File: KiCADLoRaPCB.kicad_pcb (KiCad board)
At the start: 2 copper layers, 114.8 x 85.1 mm, 16 parts, among them J1 Raspberry_Pi_2_3, J2 RHF-GW, J3 Jack-DC, J9 RHF-GWx, M5 3.2mm

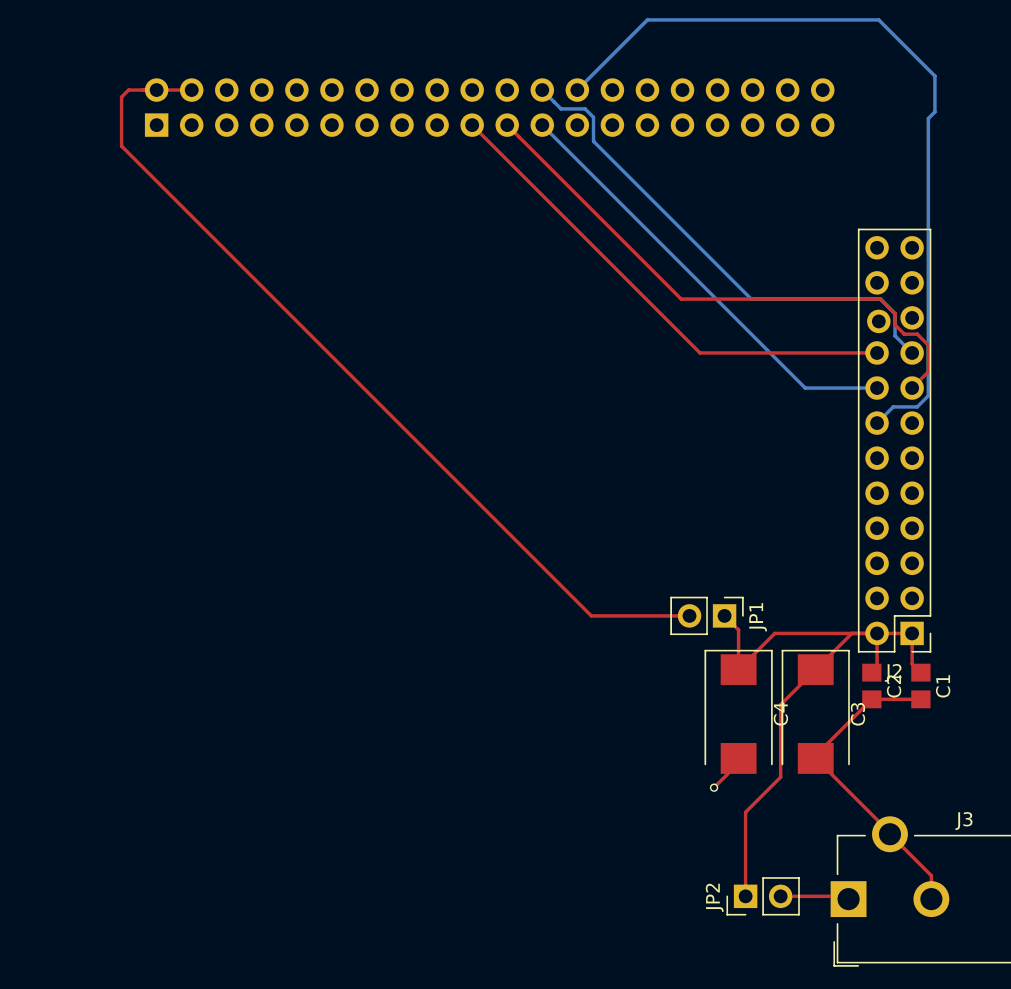
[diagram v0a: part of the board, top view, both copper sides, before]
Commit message: Finished tweaking the PWR plane and track width
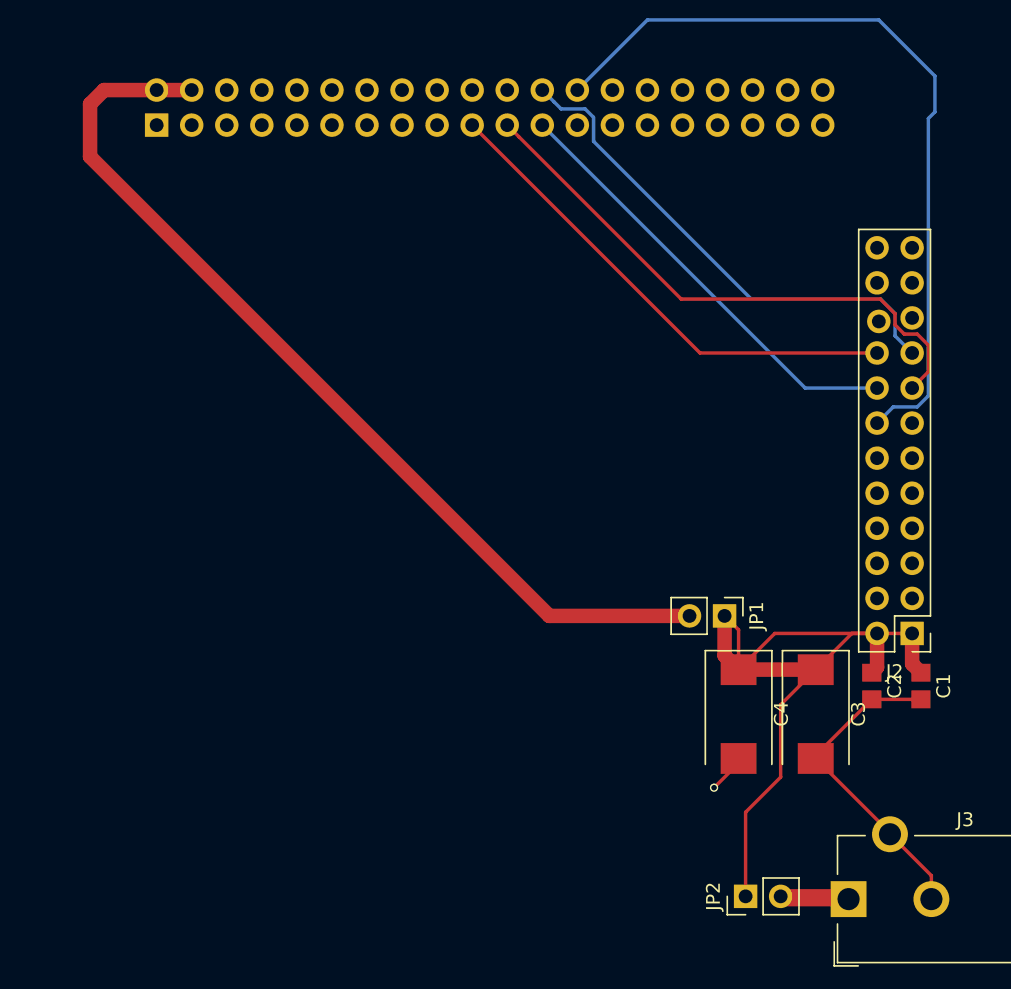
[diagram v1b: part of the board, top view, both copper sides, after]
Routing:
- net +5V: track 48.1 -> 59.5 mm
- net Net-(J3-Pad1): track 5.00 -> 10.3 mm
- net /5VR: track 65.6 -> 70.3 mm
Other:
- net class pwrr added: clearance 0.2, trace_width 1.05, via_dia 0.6, via_drill 0.4
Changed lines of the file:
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@@
     (thickness 1.6)
     (drawings 2970)
-    (tracks 69)
+    (tracks 77)
     (zones 0)
     (modules 16)
@@
     (uvia_dia 0.3)
     (uvia_drill 0.1)
-    (add_net +5V)
-    (add_net /5VR)
     (add_net GND)
     (add_net "Net-(J1-Pad1)")
@@
     (add_net "Net-(J2-Pad8)")
     (add_net "Net-(J2-Pad9)")
-    (add_net "Net-(J3-Pad1)")
   )
   (net_class SPI ""
@@
     (add_net "Net-(J1-Pad23)")
   )
+  (net_class pwrr ""
+    (clearance 0.2)
+    (trace_width 1.05)
+    (via_dia 0.6)
+    (via_drill 0.4)
+    (uvia_dia 0.3)
+    (uvia_drill 0.1)
+    (add_net +5V)
+    (add_net /5VR)
+    (add_net "Net-(J3-Pad1)")
+  )
   (module Connector_BarrelJack:BarrelJack_CUI_PJ-102AH_Horizontal placed (layer F.Cu)
     (at 137 114.5 90)
@@
   (gr_line (start 64.77 58.42) (end 60.96 58.42) (angle 90) (layer Edge.Cuts) (width 0.15))
   (gr_line (start 60.96 55.88) (end 64.77 55.88) (angle 90) (layer Edge.Cuts) (width 0.15))
+  (segment (start 129.032 97.8745) (end 134.62 97.8745) (width 1.05) (layer F.Cu) (net 1))
+  (segment (start 128.016 93.98) (end 128.016 96.8585) (width 1.05) (layer F.Cu) (net 1))
+  (segment (start 128.016 96.8585) (end 129.032 97.8745) (width 1.05) (layer F.Cu) (net 1))
+  (segment (start 141.605 95.25) (end 141.605 97.4575) (width 1.05) (layer F.Cu) (net 1))
+  (segment (start 141.605 97.4575) (end 142.24 98.0925) (width 1.05) (layer F.Cu) (net 1))
+  (segment (start 139.065 95.25) (end 139.065 97.7115) (width 1.05) (layer F.Cu) (net 1))
+  (segment (start 139.065 97.7115) (end 138.684 98.0925) (width 1.05) (layer F.Cu) (net 1))
   (segment (start 139.065 95.25) (end 141.605 95.25) (width 0.25) (layer F.Cu) (net 1))
   (segment (start 128.016 93.98) (end 129.032 94.996) (width 0.25) (layer F.Cu) (net 1))
   (segment (start 129.032 94.996) (end 129.032 97.8745) (width 0.25) (layer F.Cu) (net 1))
   (segment (start 129.54 114.3) (end 129.54 108.204) (width 0.25) (layer F.Cu) (net 1))
-  (segment (start 132.08 100.4145) (end 134.62 97.8745) (width 0.25) (layer F.Cu) (net 1))
-  (segment (start 132.08 105.664) (end 132.08 100.4145) (width 0.25) (layer F.Cu) (net 1))
   (segment (start 129.54 108.204) (end 132.08 105.664) (width 0.25) (layer F.Cu) (net 1))
+  (segment (start 132.08 105.664) (end 132.08 100.4145) (width 0.25) (layer F.Cu) (net 1))
+  (segment (start 132.08 100.4145) (end 134.62 97.8745) (width 0.25) (layer F.Cu) (net 1))
   (segment (start 139.065 95.25) (end 131.6565 95.25) (width 0.25) (layer F.Cu) (net 1))
   (segment (start 131.6565 95.25) (end 129.032 97.8745) (width 0.25) (layer F.Cu) (net 1))
   (segment (start 139.065 95.25) (end 137.2445 95.25) (width 0.25) (layer F.Cu) (net 1))
   (segment (start 137.2445 95.25) (end 134.62 97.8745) (width 0.25) (layer F.Cu) (net 1))
-  (segment (start 141.605 95.25) (end 141.605 97.4575) (width 0.25) (layer F.Cu) (net 1))
   (segment (start 141.605 97.4575) (end 142.24 98.0925) (width 0.25) (layer F.Cu) (net 1))
-  (segment (start 139.065 95.25) (end 139.065 97.7115) (width 0.25) (layer F.Cu) (net 1))
   (segment (start 139.065 97.7115) (end 138.684 98.0925) (width 0.25) (layer F.Cu) (net 1))
   (segment (start 122.428 55.88) (end 122.428 56.134) (width 0.25) (layer B.Cu) (net 2))
@@
   (segment (start 141.979003 78.834999) (end 142.780001 78.034001) (width 0.25) (layer B.Cu) (net 21))
   (segment (start 142.780001 78.034001) (end 142.780001 57.944001) (width 0.25) (layer B.Cu) (net 21))
-  (segment (start 132.08 114.3) (end 136.8 114.3) (width 0.25) (layer F.Cu) (net 45))
+  (segment (start 132.08 114.3) (end 136.8 114.3) (width 1.05) (layer F.Cu) (net 45) (status C00000))
+  (segment (start 136.8 114.3) (end 137 114.5) (width 1.05) (layer F.Cu) (net 45) (status C00000))
+  (segment (start 137 114.5) (end 132.28 114.5) (width 1.05) (layer F.Cu) (net 45) (status C00000))
+  (segment (start 132.28 114.5) (end 132.08 114.3) (width 1.05) (layer F.Cu) (net 45) (status C00000))
   (segment (start 136.8 114.3) (end 137 114.5) (width 0.25) (layer F.Cu) (net 45))
-  (segment (start 125.476 93.98) (end 118.364 93.98) (width 0.25) (layer F.Cu) (net 46))
-  (segment (start 84.836 55.88) (end 86.868 55.88) (width 0.25) (layer F.Cu) (net 46))
-  (segment (start 118.364 93.98) (end 84.328 59.944) (width 0.25) (layer F.Cu) (net 46))
-  (segment (start 84.328 59.944) (end 84.328 56.388) (width 0.25) (layer F.Cu) (net 46))
-  (segment (start 84.328 56.388) (end 84.836 55.88) (width 0.25) (layer F.Cu) (net 46))
+  (segment (start 86.868 55.88) (end 83.058 55.88) (width 1.05) (layer F.Cu) (net 46))
+  (segment (start 83.058 55.88) (end 82.042 56.896) (width 1.05) (layer F.Cu) (net 46))
+  (segment (start 82.042 56.896) (end 82.042 60.706) (width 1.05) (layer F.Cu) (net 46))
+  (segment (start 82.042 60.706) (end 115.316 93.98) (width 1.05) (layer F.Cu) (net 46))
+  (segment (start 115.316 93.98) (end 125.476 93.98) (width 1.05) (layer F.Cu) (net 46))
+  (segment (start 86.868 55.88) (end 89.408 55.88) (width 1.05) (layer F.Cu) (net 46))
   (segment (start 86.868 55.88) (end 85.852 55.88) (width 0.25) (layer F.Cu) (net 46))
   (segment (start 86.868 55.88) (end 86.36 55.88) (width 0.25) (layer F.Cu) (net 46))
-  (segment (start 89.408 55.88) (end 86.868 55.88) (width 0.25) (layer F.Cu) (net 46))
   (zone (net 2) (net_name GND) (layer B.Cu) (hatch edge 0.508)
     (connect_pads (clearance 0.508))

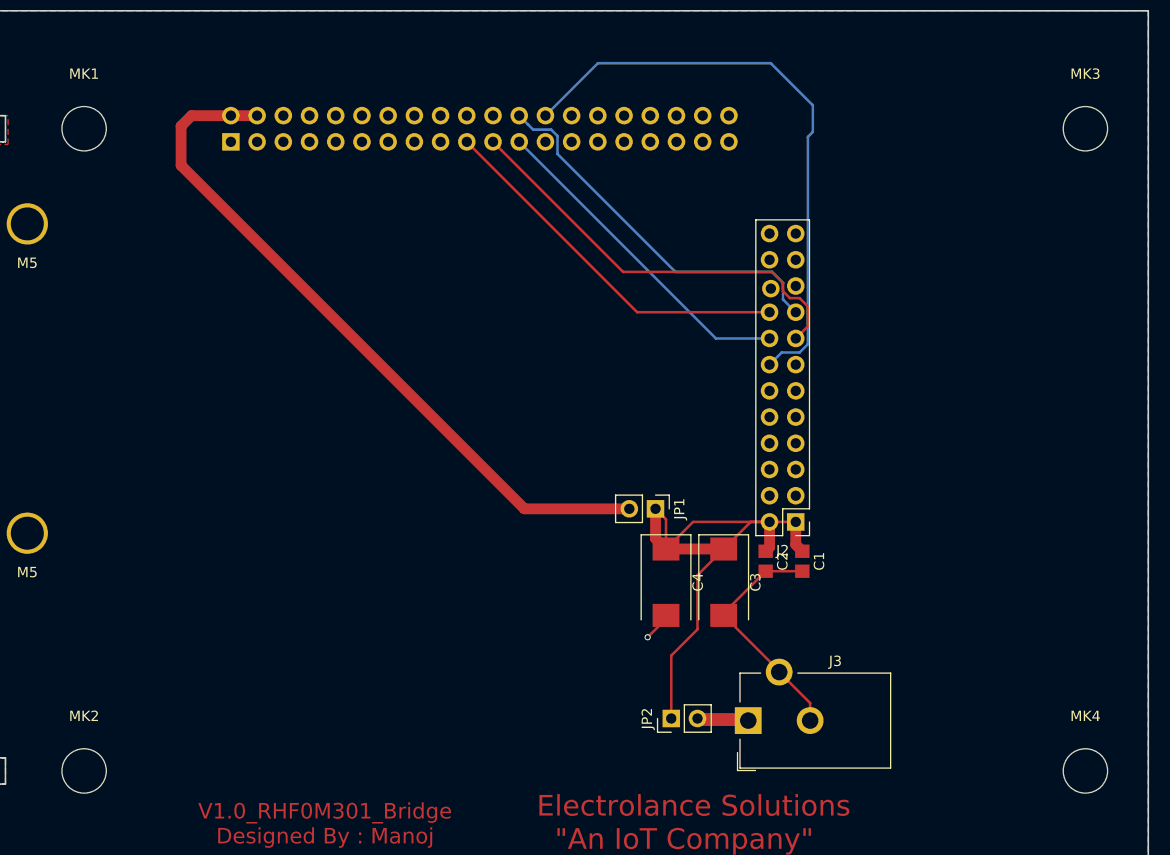
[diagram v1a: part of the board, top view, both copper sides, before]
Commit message: Etching round design
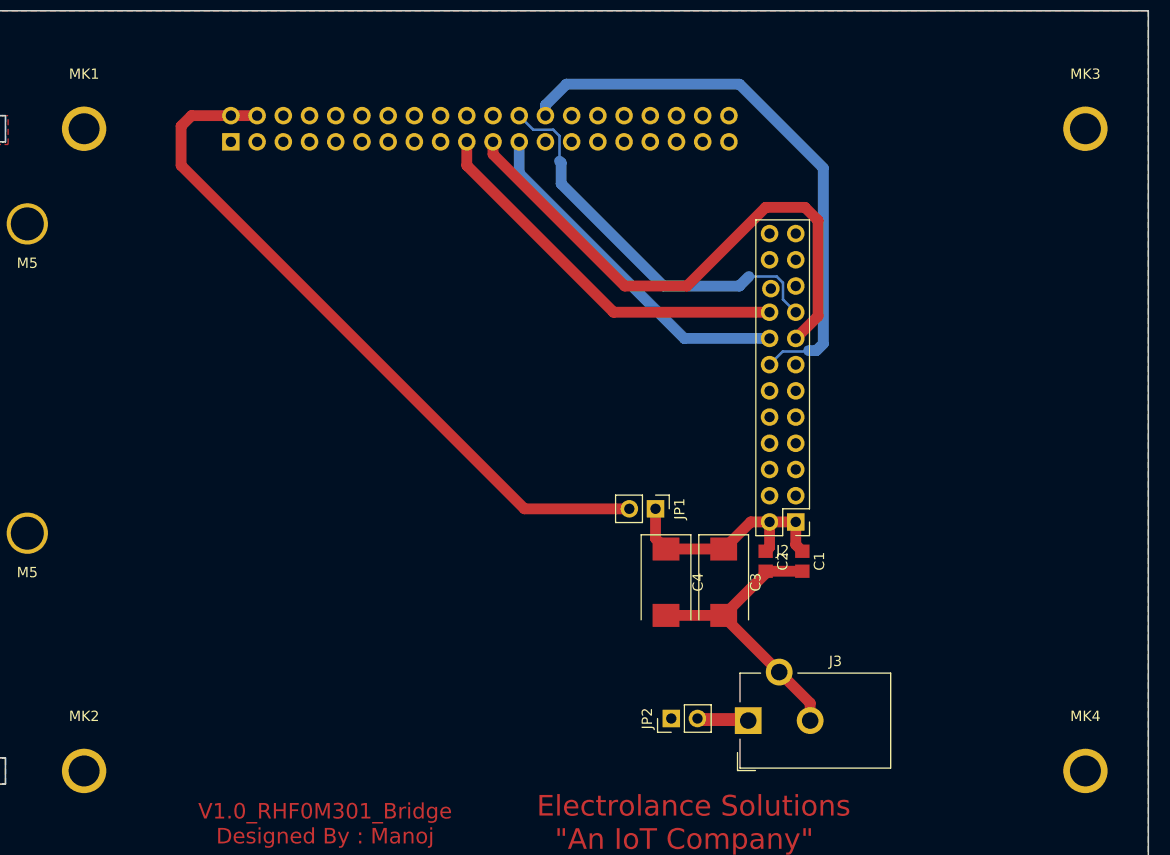
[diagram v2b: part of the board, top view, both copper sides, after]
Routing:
- net +5V: track 59.5 -> 25.5 mm
- net Net-(J1-Pad21): track 41.2 -> 54.0 mm
- net GND: track 26.3 -> 29.7 mm, vias 1 -> 0
- net Net-(J1-Pad26): track 57.6 -> 55.1 mm
- net Net-(J1-Pad24): track 36.7 -> 39.0 mm
- net Net-(J1-Pad23): track 32.1 -> 33.9 mm
- net Net-(J1-Pad19): track 36.2 -> 37.5 mm
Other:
- net class SPI: trace_width 0.25 -> 0.5
